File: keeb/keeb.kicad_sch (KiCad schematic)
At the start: 162 parts, among them J101 USB_C_Receptacle_USB2.0, J102 AVR-ISP-6, SW101 SW_Push, SW102 SW_Push, SW103 SW_Push, SW104 SW_Push, SW105 SW_Push, SW106 SW_Push, SW107 SW_Push, SW108 SW_Push, SW109 SW_Push, SW110 SW_Push, SW111 SW_Push, SW112 SW_Push, SW113 SW_Push, SW114 SW_Push, SW115 SW_Push, SW116 SW_Push, SW117 SW_Push, SW118 SW_Push, SW119 SW_Push, SW120 SW_Push, SW121 SW_Push, SW122 SW_Push, SW123 SW_Push, SW124 SW_Push, SW125 SW_Push, SW126 SW_Push, SW127 SW_Push, SW128 SW_Push, SW129 SW_Push, SW130 SW_Push, SW131 SW_Push, SW132 SW_Push, SW133 SW_Push, SW134 SW_Push, SW135 SW_Push, SW136 SW_Push, SW137 SW_Push, SW138 SW_Push, SW139 SW_Push, SW140 SW_Push, SW141 SW_Push, SW142 SW_Push, SW143 SW_Push, SW144 SW_Push, SW145 SW_Push, SW146 SW_Push, SW147 SW_Push, SW148 SW_Push, SW149 SW_Push, SW150 SW_Push, SW151 SW_Push, SW152 SW_Push, SW153 SW_Push, SW154 SW_Push, SW155 SW_Push, SW156 SW_Push, SW157 SW_Push, SW158 SW_Push, SW159 SW_Push, SW160 SW_Push, SW161 SW_Push, SW162 SW_Push, SW163 SW_Push, SW164 SW_Push, SW165 SW_Push, SW166 SW_Push, SW167 SW_Push, U101 TPD2S017, U102 ATmega32U4-AU, Y101 16Mhz

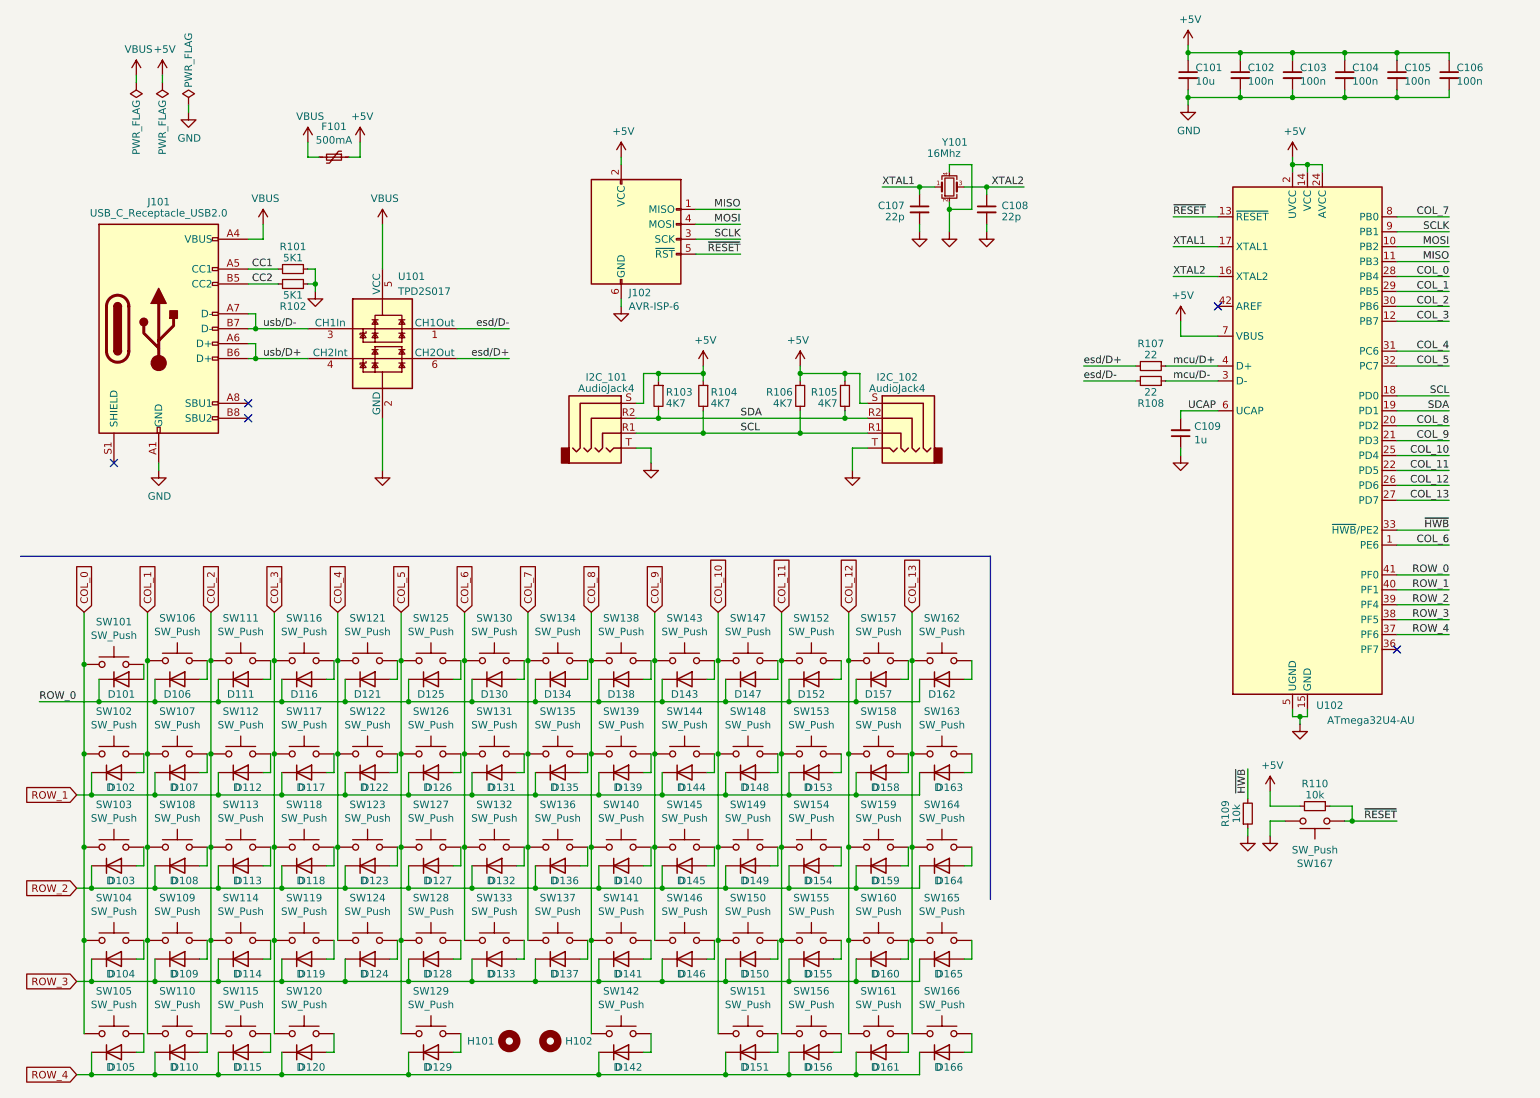
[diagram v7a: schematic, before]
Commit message: usb/matrix/mcu routing
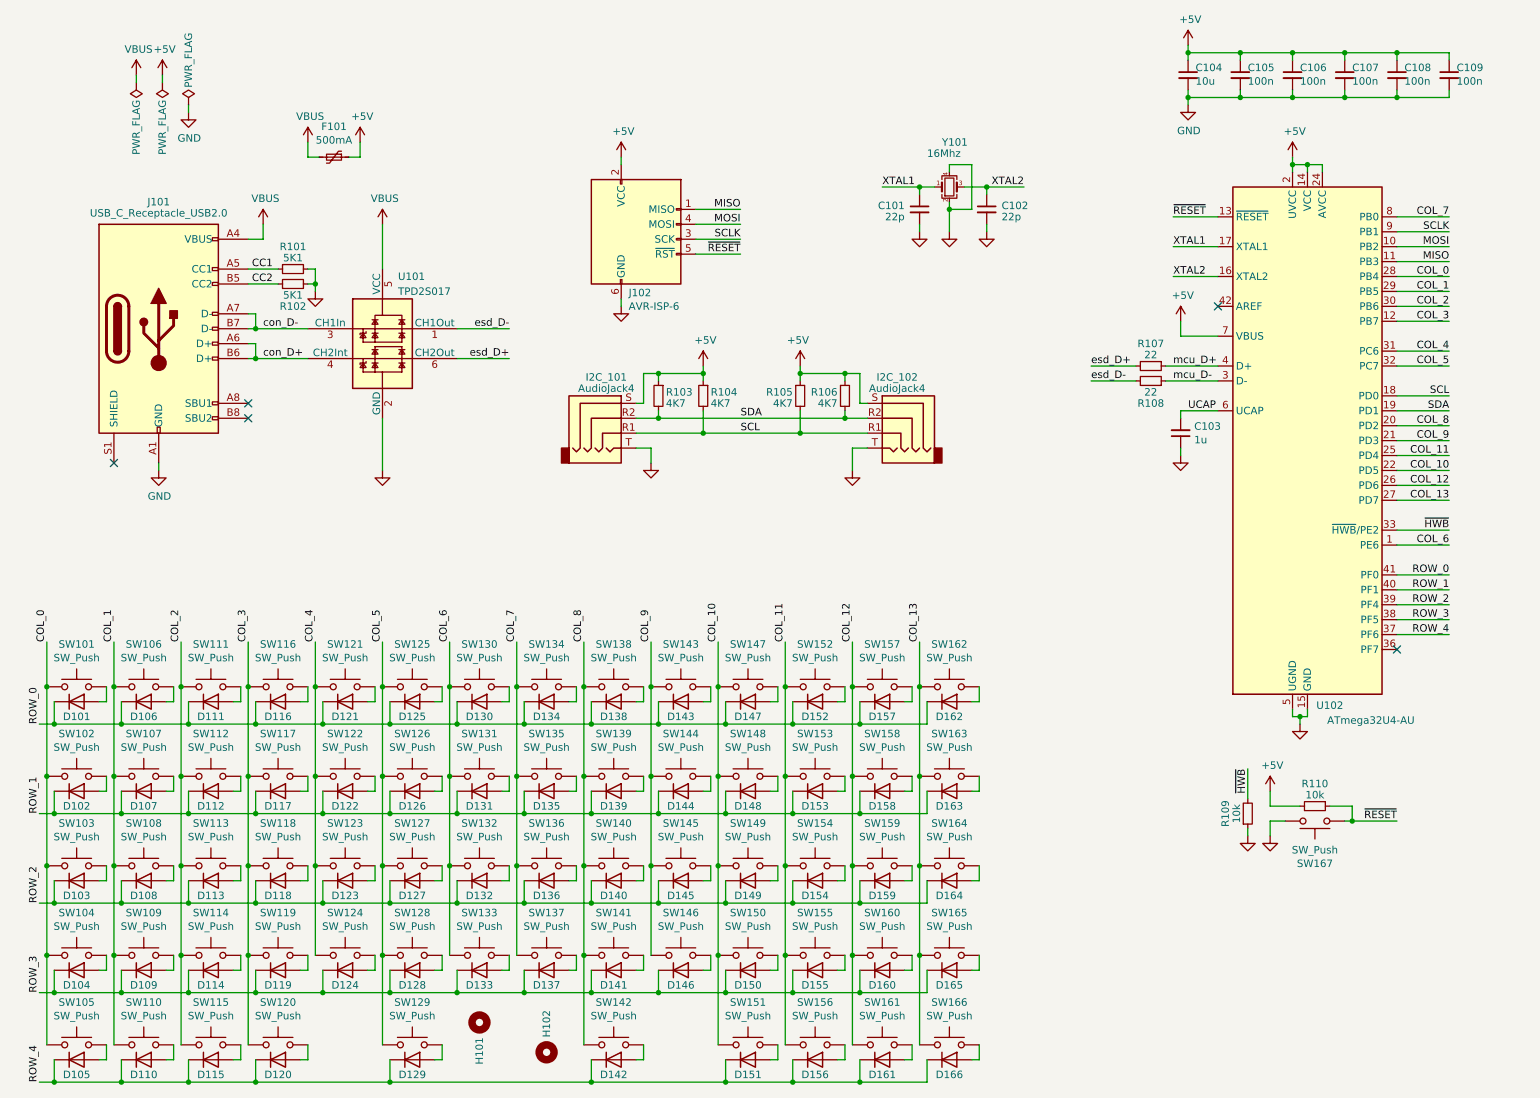
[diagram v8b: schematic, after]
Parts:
- SW129, SW142: footprint PCM_Switch_Keyboard_Cherry_MX:SW_Cherry_MX_PCB_3.00u -> PCM_Switch_Keyboard_Cherry_MX:SW_Cherry_MX_PCB_1.00u
- U102: symbol MCU_Microchip_ATmega:ATmega32U4RC-A -> MCU_Microchip_ATmega:ATmega32U4-M
- Y101: LCSC (none) -> https://www.lcsc.com/product-detail/Crystals_YLFailong-Crys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; LCSC# (none) -> C431146; Supplier # LCSC: C431146 -> (none)
- renumbered C107 to C101, C108 to C102, C109 to C103, C101 to C104, C102 to C105, C103 to C106, C104 to C107, C105 to C108, C106 to C109, R106 to R105, R105 to R106
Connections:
- net COL_10: now also U102.22 (PD5); no longer U102.25 (PD4)
- net COL_11: now also U102.25 (PD4); no longer U102.22 (PD5)
- net GND: now also U102.45 (GND)
- net esd/D+ renamed esd_D+
- net esd/D- renamed esd_D-
- net mcu/D+ renamed mcu_D+
- net mcu/D- renamed mcu_D-
- net usb/D+ renamed con_D+
- net usb/D- renamed con_D-
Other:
- moved on the sheet: H101, H102
